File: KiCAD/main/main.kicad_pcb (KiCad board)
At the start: 2 copper layers, 76 x 60.5 mm, 24 parts, among them IC1 DHT22, J1 Sound Sensor, J2 BuckConverter, J3 Charge Controller, J4 Battery Status, J5 Anemometer, J6 Conn_02x04_Odd_Even, SW1 SW_SPDT, SW2 BOOT, SW3 RESET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

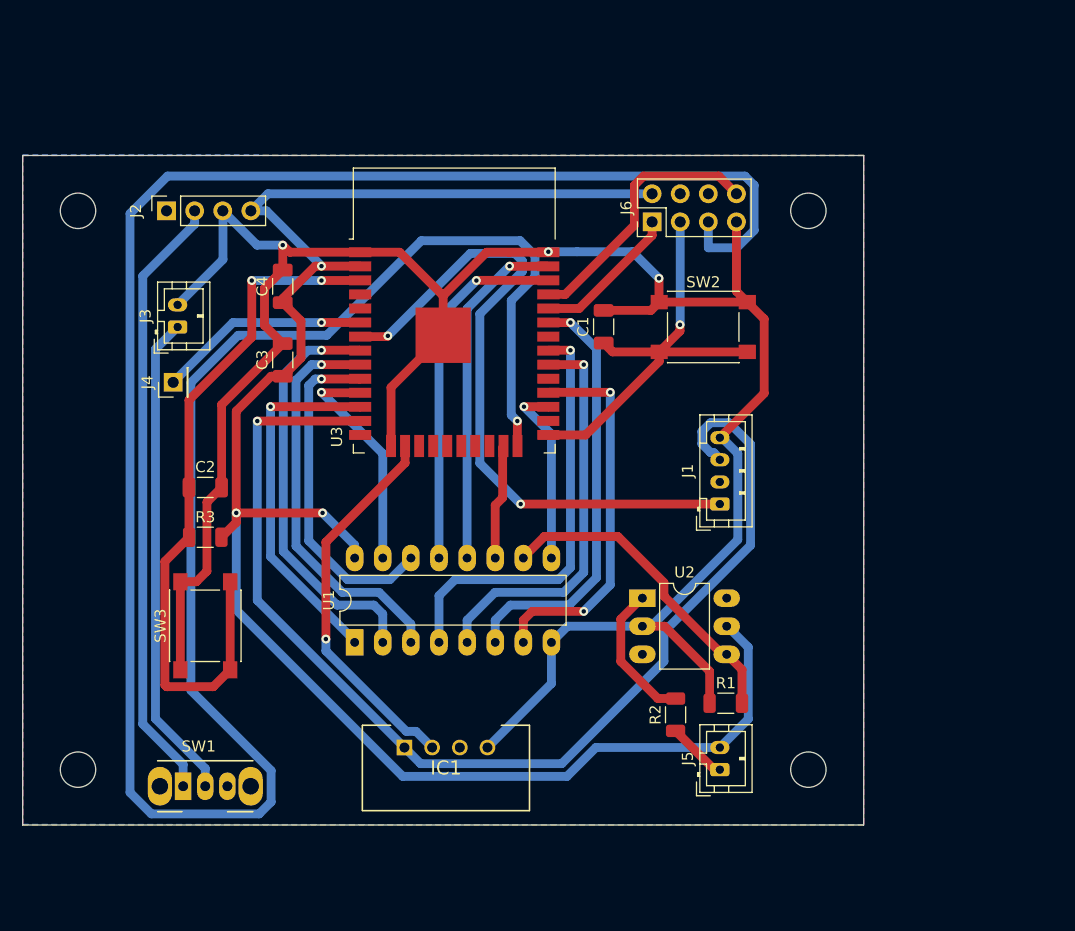
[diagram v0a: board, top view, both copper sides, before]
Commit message: Adjust via size and decrease clearance to 0.3mm
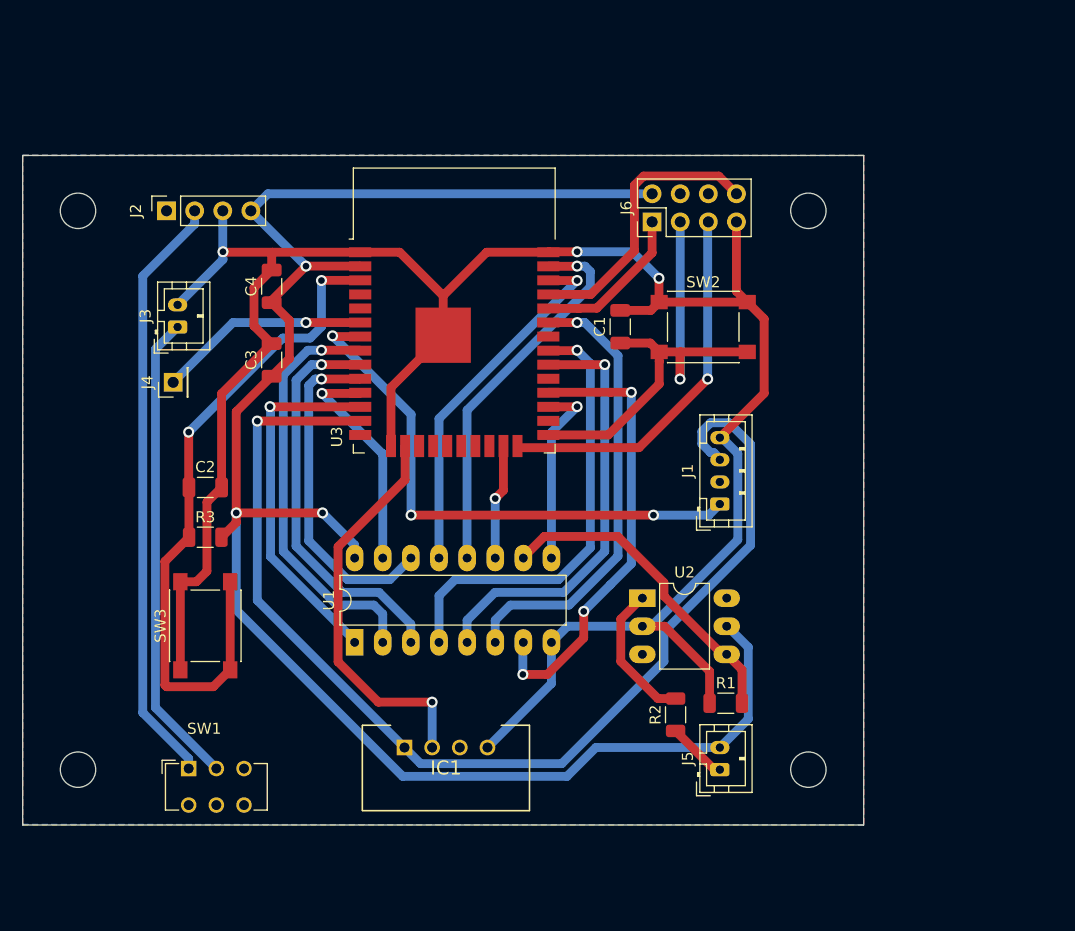
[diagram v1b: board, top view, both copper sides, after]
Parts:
- SW1: footprint Button_Switch_THT:SW_CuK_OS102011MA1QN1_SPDT_Angled -> Button_Switch_THT:SW_CuK_JS202011AQN_DPDT_Angled
- moved SW1 1.68 mm to (108.0, 117.4)
- moved C1 1.50 mm to (147.0, 77.5)
- moved C3 1.00 mm to (115.5, 80.5)
- moved C4 1.00 mm to (115.5, 73.8)
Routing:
- net /Microcontroller/IO2: track 231.9 -> 34.0 mm
- net /Sound_Signal: track 61.1 -> 50.0 mm, vias 2 -> 3
- net /Microcontroller/IO17: track 34.2 -> 41.3 mm, vias 2 -> 3
- net GND: track 206.3 -> 202.2 mm
- net /Microcontroller/IO0: track 39.5 -> 43.3 mm
- net /Microcontroller/IO23: track 31.5 -> 34.5 mm
- net /Microcontroller/IO18: track 36.3 -> 39.0 mm
- net /Microcontroller/I021: track 38.8 -> 41.2 mm
- net /Microcontroller/EN: track 64.2 -> 62.0 mm
- net /Microcontroller/IO19: track 38.8 -> 40.7 mm
- net +3V3: track 165.1 -> 163.6 mm
- net /DHT22_Data: track 34.7 -> 36.1 mm
- net /Vin_Buck: track 55.5 -> 54.1 mm
- net /Microcontroller/TXD0: track 24.2 -> 25.6 mm
- net Net-(J3-Pad1): track 44.2 -> 43.0 mm
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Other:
- net class Default: clearance 0.35 -> 0.3
- rule trace_clearance: 0.35 -> 0.3

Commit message: Add some pcb test points
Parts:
- added TP1: Batt_status, TestPoint:TestPoint_Pad_1.0x1.0mm, F.Cu at (105.0, 87.0)
- added TP2: Vin_Buck, TestPoint:TestPoint_Pad_1.0x1.0mm, F.Cu at (108.5, 70.7)
- added TP3: GND, TestPoint:TestPoint_Pad_1.0x1.0mm, F.Cu at (162.0, 89.0)
- added TP4: VDD, TestPoint:TestPoint_Pad_1.0x1.0mm, F.Cu at (162.0, 97.0)
- added TP5: supply_on, TestPoint:TestPoint_Pad_1.0x1.0mm, F.Cu at (162.0, 93.0)
- added TP6: Anemometer_Out, TestPoint:TestPoint_Pad_1.0x1.0mm, F.Cu at (162.0, 101.0)
- added TP7: EN, TestPoint:TestPoint_Pad_1.0x1.0mm, F.Cu at (114.2, 112.3)
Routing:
- net /Anemometer_Out: track 5.45 -> 24.9 mm
- net +3V3: track 163.6 -> 173.3 mm
- net /supply_on: track 104.0 -> 111.4 mm
- net GND: track 202.2 -> 208.6 mm
- net /Battery_status: track 19.1 -> 24.3 mm
- net /Microcontroller/EN: track 62.0 -> 66.8 mm
- net /Vin_Buck: track 54.1 -> 57.8 mm

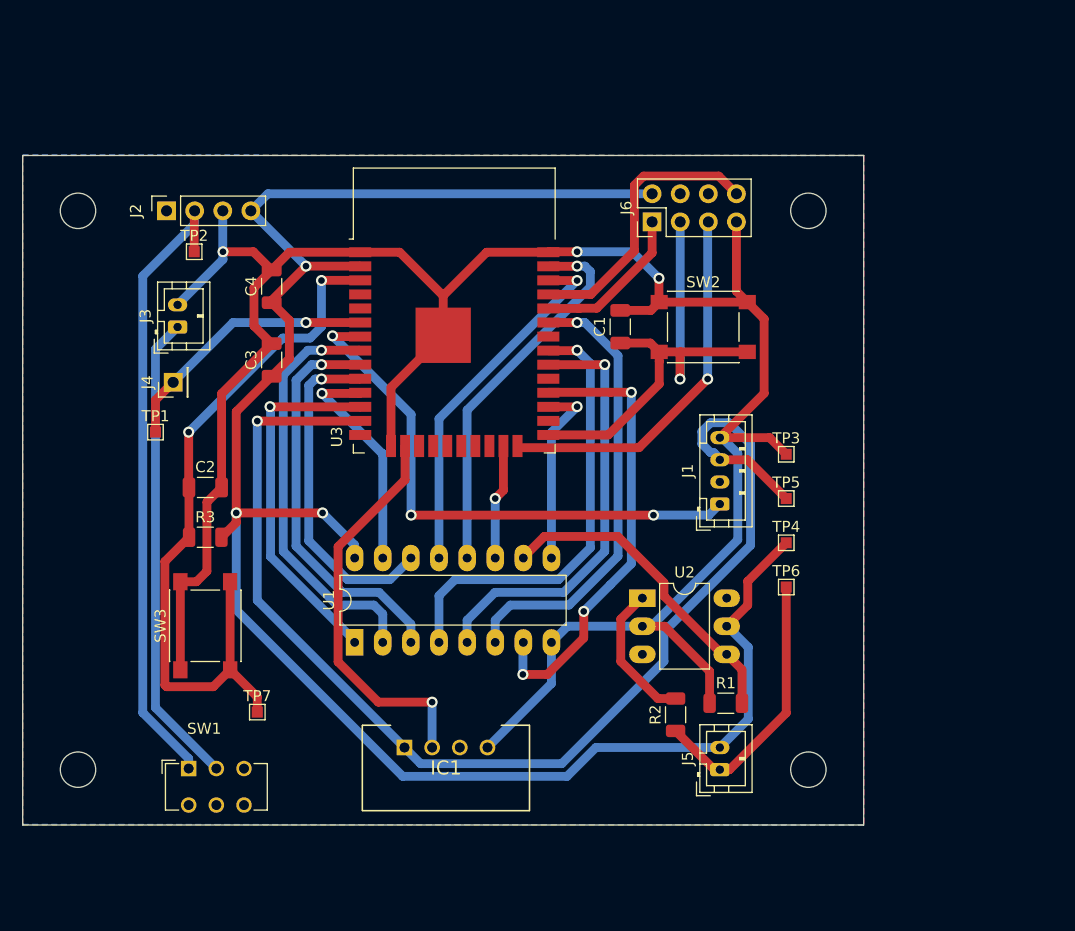
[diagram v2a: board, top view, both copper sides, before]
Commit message: Replace all possible footprints to THT variants
Also clear current PCB design and update component footprints
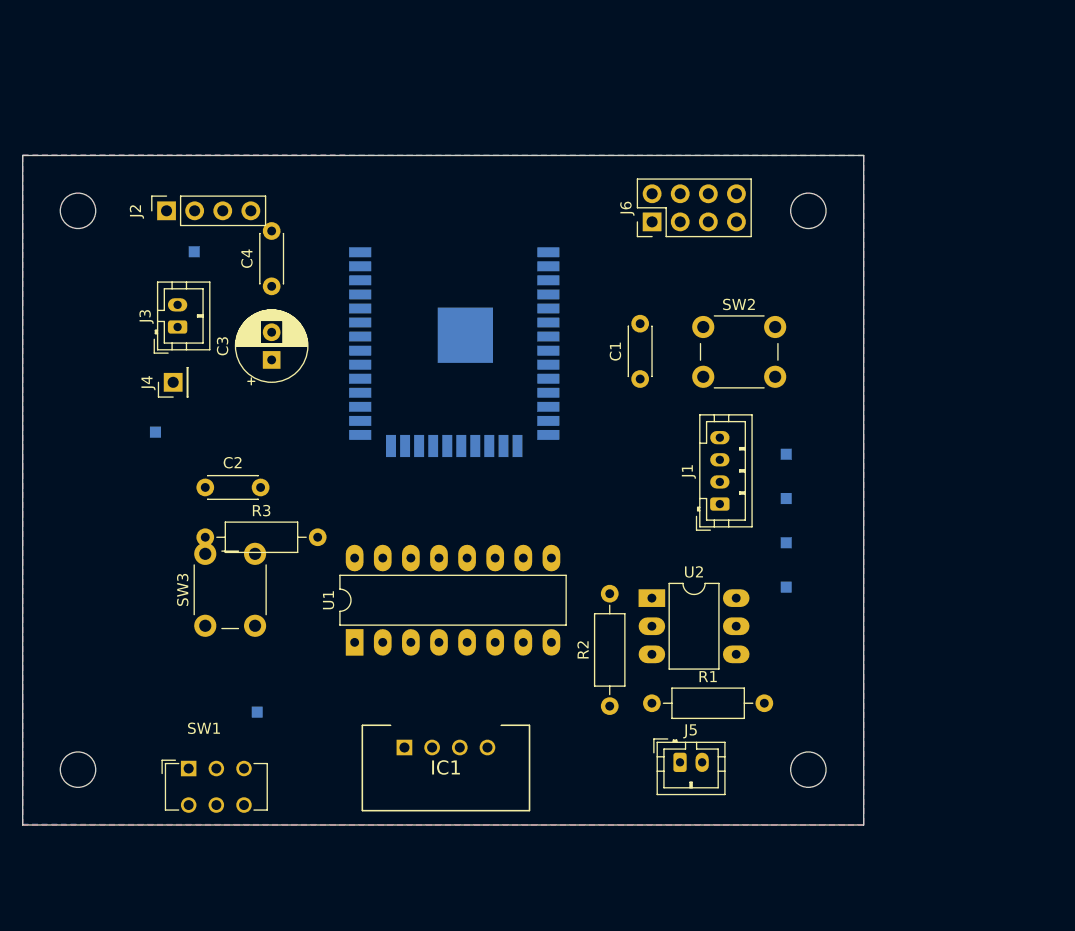
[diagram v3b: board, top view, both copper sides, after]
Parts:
- C1, C2, C4: footprint Capacitor_SMD:C_1206_3216Metric -> Capacitor_THT:C_Disc_D4.3mm_W1.9mm_P5.00mm
- C3: footprint Capacitor_SMD:C_1206_3216Metric -> Capacitor_THT:CP_Radial_D6.3mm_P2.50mm
- R1, R2, R3: footprint Resistor_SMD:R_1206_3216Metric -> Resistor_THT:R_Axial_DIN0207_L6.3mm_D2.5mm_P10.16mm_Horizontal
- SW2, SW3: footprint Button_Switch_SMD:SW_SPST_PTS645 -> Button_Switch_THT:SW_PUSH_6mm
- TP1, TP2, TP3, TP4, TP5, TP6, TP7, U3: moved to B.Cu
- moved R1 6.68 mm to (149.9, 111.5)
- moved R2 6.00 mm to (146.1, 111.8)
- moved C1 5.06 mm to (148.8, 82.2)
- moved J5 3.66 mm to (152.4, 116.8), turned to 0 degrees
- moved U2 0.86 mm to (149.9, 102.0)
- turned U3 to 180 degrees
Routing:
- net GND: track 208.6 -> 0.00 mm, vias 3 -> 0
- net +3V3: track 173.3 -> 0.00 mm, vias 3 -> 0
- net /supply_on: track 111.4 -> 0.00 mm, vias 1 -> 0
- net /Microcontroller/EN: track 66.8 -> 0.00 mm, vias 2 -> 0
- net /Vin_Buck: track 57.8 -> 0.00 mm
- net /Sound_Signal: track 50.0 -> 0.00 mm, vias 3 -> 0
- net /Microcontroller/IO0: track 43.3 -> 0.00 mm, vias 1 -> 0
- net Net-(J3-Pad1): track 43.0 -> 0.00 mm
- net /Microcontroller/IO17: track 41.3 -> 0.00 mm, vias 3 -> 0
- net /Microcontroller/I021: track 41.2 -> 0.00 mm, vias 1 -> 0
- net /Microcontroller/IO19: track 40.7 -> 0.00 mm, vias 1 -> 0
- net /Microcontroller/IO18: track 39.0 -> 0.00 mm, vias 1 -> 0
- net /Microcontroller/IO32: track 37.7 -> 0.00 mm, vias 1 -> 0
- net /Microcontroller/IO33: track 36.3 -> 0.00 mm, vias 1 -> 0
- net /DHT22_Data: track 36.1 -> 0.00 mm, vias 1 -> 0
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
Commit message: Expand design vertically, reposition components and re-track
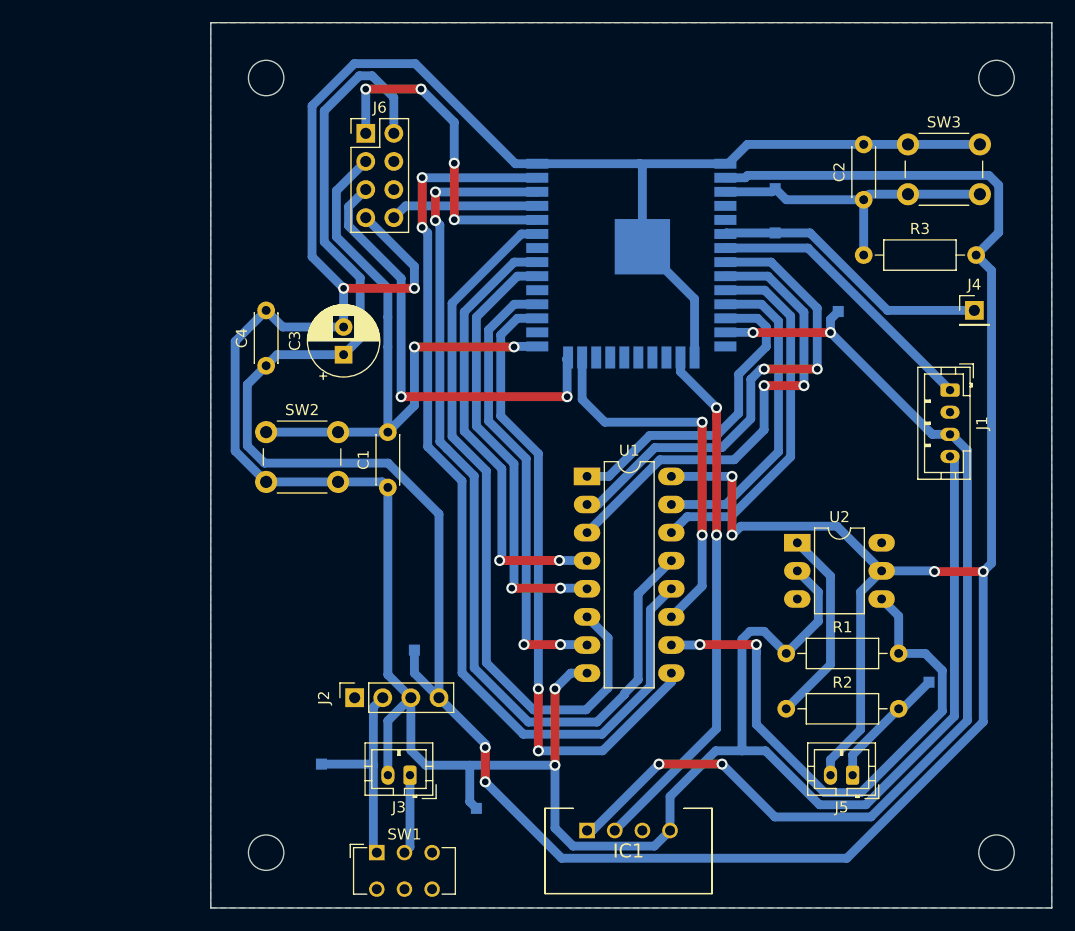
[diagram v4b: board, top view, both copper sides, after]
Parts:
- removed the REF** at (164.0, 117.5)
- removed the REF** at (98.0, 117.5)
- removed the REF** at (98.0, 67.0)
- added REF**: MountingHole_3.2mm_M3, MountingHole:MountingHole_3.2mm_M3, F.Cu at (115.0, 55.0)
- added REF**: MountingHole_3.2mm_M3, MountingHole:MountingHole_3.2mm_M3, F.Cu at (181.0, 125.0)
- added REF**: MountingHole_3.2mm_M3, MountingHole:MountingHole_3.2mm_M3, F.Cu at (115.0, 125.0)
- moved SW3 77.0 mm to (173.0, 61.0), turned to 0 degrees
- moved J4 72.7 mm to (179.0, 76.0), turned to 0 degrees
- moved TP7 66.5 mm to (161.0, 65.0), turned to 180 degrees
- moved C2 64.9 mm to (169.0, 66.0), turned to 90 degrees
- moved R3 64.7 mm to (169.0, 71.0)
- moved TP1 58.8 mm to (161.0, 69.0), turned to 270 degrees
- moved TP2 47.7 mm to (120.0, 117.0), turned to 180 degrees
- moved J2 47.2 mm to (123.0, 111.0)
- moved J3 45.6 mm to (128.0, 118.0), turned to 180 degrees
- moved TP3 42.5 mm to (134.0, 121.0), turned to 270 degrees
- moved SW2 40.6 mm to (115.0, 87.0)
- moved TP4 35.0 mm to (128.4, 106.7), turned to 270 degrees
- moved J6 27.1 mm to (124.0, 60.0), turned to 0 degrees
- moved U1 25.8 mm to (144.0, 91.0), turned to 0 degrees
- moved C1 24.8 mm to (126.0, 92.0)
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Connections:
- C1 pad 1: /Microcontroller/IO0 -> GND
- C1 pad 2: GND -> /Microcontroller/IO0
- R2 pad 1: /Anemometer_Out -> Net-(R2-Pad1)
- R2 pad 2: Net-(R2-Pad2) -> /Anemometer_Out
- SW2 pad 1: GND -> /Microcontroller/IO0
- SW2 pad 2: /Microcontroller/IO0 -> GND
- U2 pad 1: Net-(R2-Pad2) -> Net-(R2-Pad1)
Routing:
- net GND: track 0.00 -> 320.8 mm, vias 0 -> 4
- net +3V3: track 0.00 -> 286.3 mm, vias 0 -> 6
- net /supply_on: track 0.00 -> 95.3 mm, vias 0 -> 4
- net /Microcontroller/IO23: track 0.00 -> 87.3 mm, vias 0 -> 2
- net /Microcontroller/IO22: track 0.00 -> 84.1 mm, vias 0 -> 2
- net /Microcontroller/I021: track 0.00 -> 64.8 mm
- net /Microcontroller/IO16: track 0.00 -> 58.3 mm, vias 0 -> 2
- net /Microcontroller/IO0: track 0.00 -> 58.3 mm, vias 0 -> 2
- net /Opto_Anemometer_Out: track 0.00 -> 51.1 mm, vias 0 -> 2
- net /DHT22_Data: track 0.00 -> 47.9 mm, vias 0 -> 2
- net /Microcontroller/IO32: track 0.00 -> 43.5 mm, vias 0 -> 2
- net /Microcontroller/IO33: track 0.00 -> 42.5 mm, vias 0 -> 2
- net /Microcontroller/IO17: track 0.00 -> 41.0 mm, vias 0 -> 2
- net /Microcontroller/IO19: track 0.00 -> 40.3 mm, vias 0 -> 2
- net /Microcontroller/IO2: track 0.00 -> 40.1 mm, vias 0 -> 2
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- removed copper zone on F.Cu, net (none)
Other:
- board size 76 x 60.5 mm -> 76 x 80 mm
- rule trace_min: 0.5 -> 0.8
- rule via_min_size: 0.4 -> 0.8
